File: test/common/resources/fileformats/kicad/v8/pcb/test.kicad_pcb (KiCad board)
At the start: 2 copper layers, 4 parts

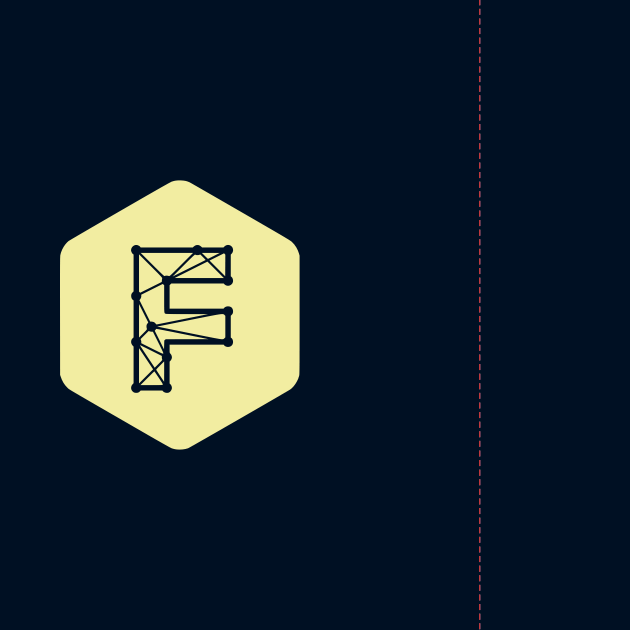
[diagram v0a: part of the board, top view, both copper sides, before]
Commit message: layout_viewer: stabilize pad annotations and improve text rendering
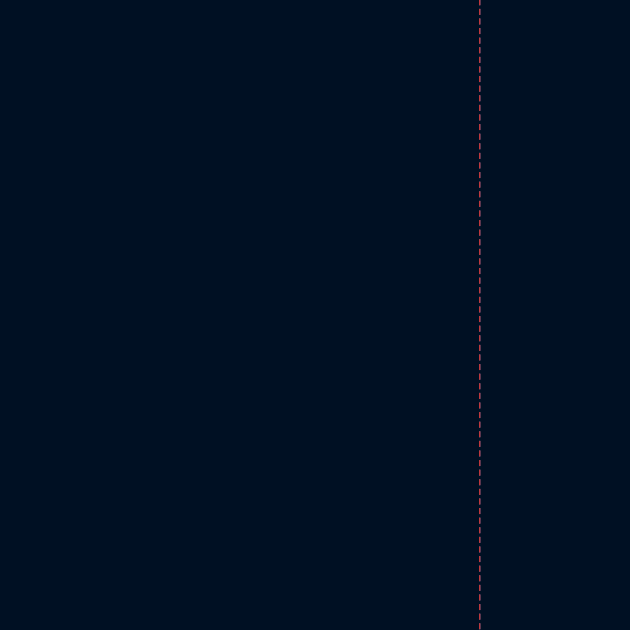
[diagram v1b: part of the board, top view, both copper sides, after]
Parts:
- G***: moved to B.Cu
- turned G*** to 270 degrees

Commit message: layout_viewer: fix TH oval annulus geometry and cleanup drill synthesis
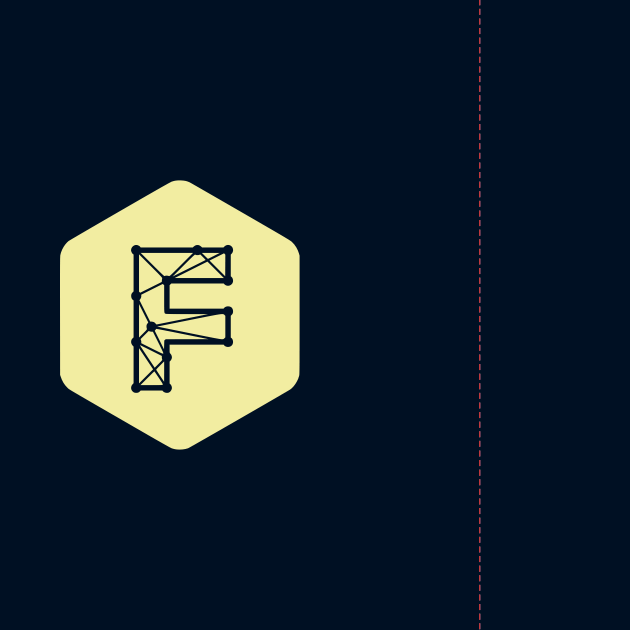
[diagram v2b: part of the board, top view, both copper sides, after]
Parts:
- G***: moved to F.Cu
- turned G*** to 0 degrees
